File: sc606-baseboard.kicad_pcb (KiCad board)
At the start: 6 copper layers, 100 x 80 mm, 479 parts, among them IC1 TPS54561DPRT, IC2 TPS7A0518PDBVT, IC3 TPS7A0518PDBVT, J1 1053131102, J10 E8124-015-01, J11 E8124-015-01, J12 E8124-015-01, J14 CONMMCX002-SMD-T, J2 WE_68715014522, J3 F52R-1A7H1-11020, J4 46756-1001, J5 U_FL-R-SMT-1_10_, J6 E8124-015-01, J7 DM3AT-SF-PEJM5, J8 693022010811, J9 E8124-015-01, M1 SC606T, Q1 BSS138APW, Q10 Si7223DN, Q11 Si7223DN, Q2 BSS138-7-F, Q3 BSS138APW, Q4 BSS138APW, Q5 BSS138APW, Q6 BSS138APW, Q7 BSS138-7-F, Q8 BSS138-7-F, Q9 SQS401EN-T1_BE3, SW1 1X03, U1 AP62301WU-7, U10 NCP163ASN330T1G, U11 EMIF06-MSD02N16, U12 STUSB4500QTR, U13 FT232RQ-REEL, U14 LTC4418IUF#PBF, U15 USB57442G, U2 AP62301WU-7, U3 AP62301WU-7, U4 74LVC1G123GN, U5 NTS0102GT, U6 PCA9547BS, U7 LT9611UXC, U8 NTS0102GT, U9 FSUSB30UMX, Y1 ABM8G-24.000MHZ-18-D2Y-T, Y2 ABM8G-25.000MHZ-B4Y-T

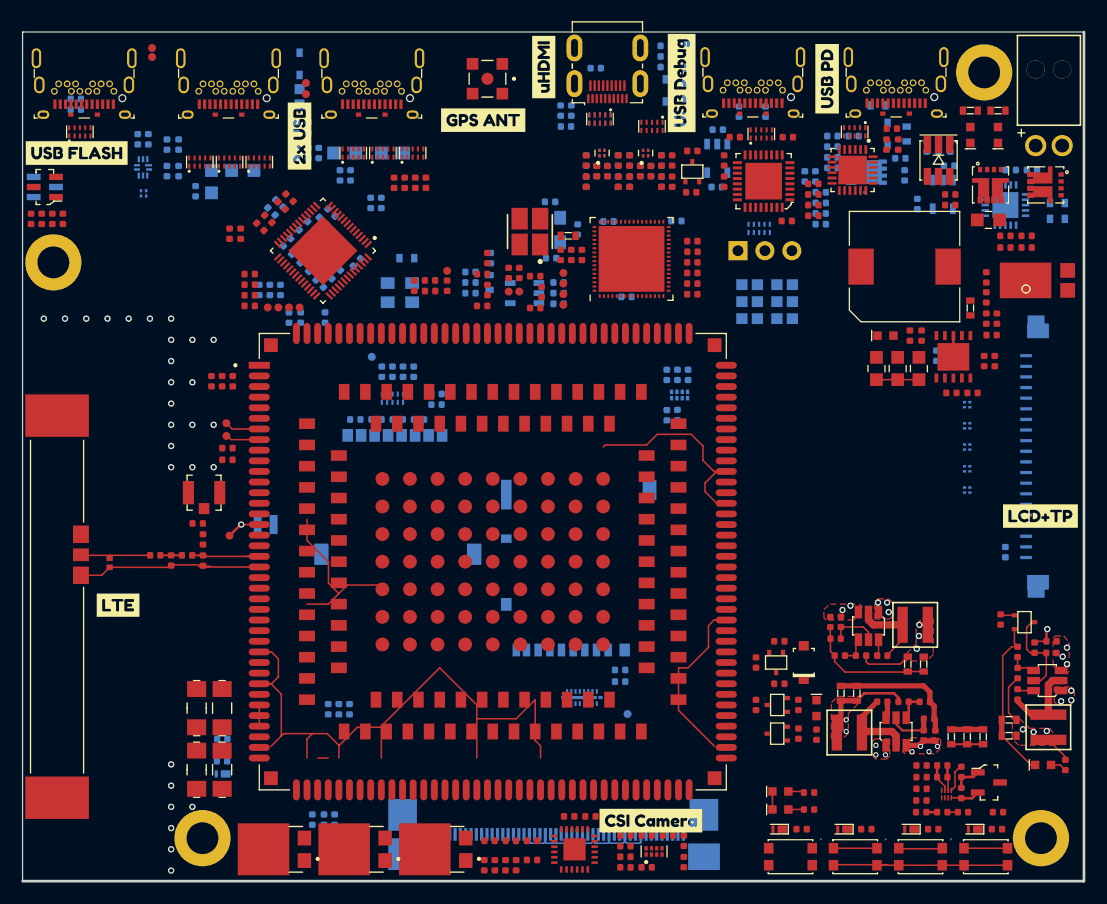
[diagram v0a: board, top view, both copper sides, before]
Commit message: Adjusted position of uHDMI
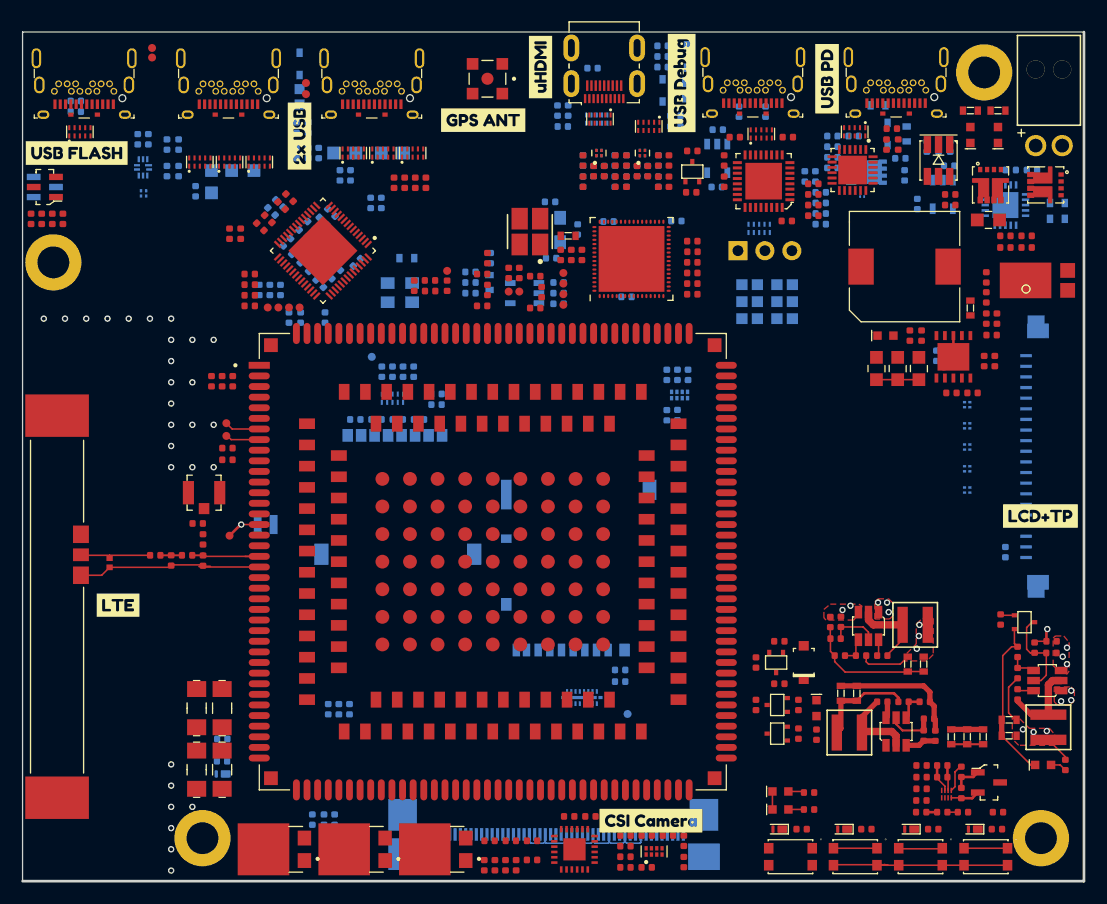
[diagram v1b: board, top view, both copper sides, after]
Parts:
- moved D35 0.40 mm to (154.7, 57.9)
- moved C75 0.30 mm to (133.5, 55.5)
- moved C76 0.30 mm to (134.5, 55.5)
- moved C77 0.30 mm to (133.5, 55.5)
- moved C78 0.30 mm to (134.5, 55.5)
- moved C81 0.30 mm to (135.5, 54.5)
- moved C82 0.30 mm to (135.5, 56.5)
- moved D30 0.30 mm to (129.7, 50.6)
- moved D6 0.30 mm to (134.6, 51.3)
- moved L18 0.30 mm to (134.0, 53.8)
- moved L19 0.30 mm to (134.0, 53.8)
- moved R61 0.30 mm to (137.1, 51.3)
- moved R62 0.30 mm to (137.1, 50.3)
- moved R64 0.30 mm to (131.4, 56.5)
- moved R67 0.30 mm to (132.5, 56.5)
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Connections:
- Q11 pad 5: (no net) -> VDD
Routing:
- net GND: track 219.1 -> 105.8 mm, vias 32 -> 29
- net (no net): track 2.00 -> 0.00 mm
- net USB_VBUS: track 1.00 -> 0.00 mm
- net 5V0_SYS: vias 9 -> 5
- net 3V3_SYS: vias 2 -> 0
- removed copper zone on F.Cu, net 3V3_SYS

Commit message: Modified position of buttons, SD, SIM and USB connectors. Modified LT9611 footprint
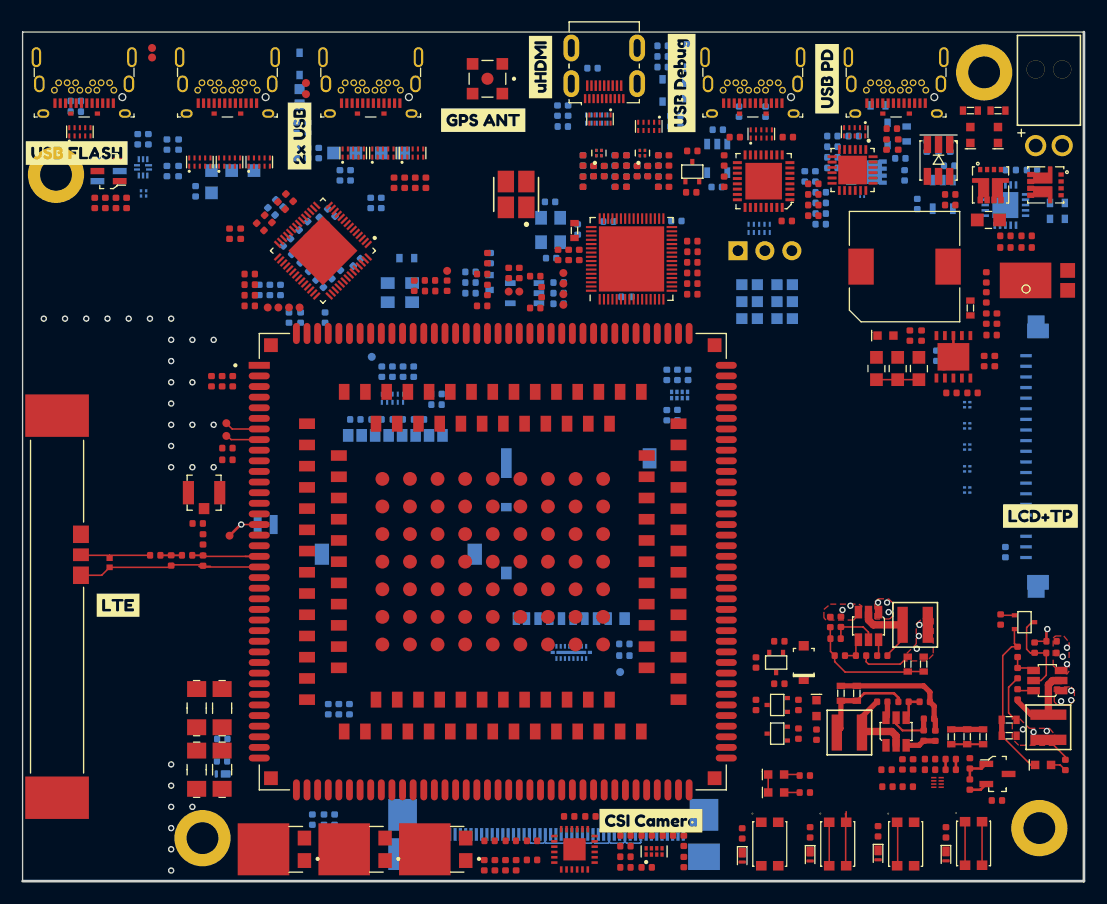
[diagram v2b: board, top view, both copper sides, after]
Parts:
- moved MP3 8.25 mm to (78.8, 55.9)
- moved Q7 6.18 mm to (83.7, 55.5)
- moved Q8 6.18 mm to (83.7, 55.5)
- moved R108 6.18 mm to (85.4, 58.5)
- moved R109 6.18 mm to (83.4, 58.5)
- moved R110 6.18 mm to (84.4, 58.5)
- moved R111 6.18 mm to (82.4, 58.5)
- moved R24 5.73 mm to (159.0, 113.5)
- moved R21 5.70 mm to (157.1, 113.5)
- moved R162 5.61 mm to (143.4, 117.9), turned to 270 degrees
- moved R96 5.31 mm to (149.8, 117.8), turned to 270 degrees
- moved R95 5.20 mm to (156.2, 117.7), turned to 270 degrees
- moved R22 5.16 mm to (157.0, 111.9), turned to 180 degrees
- moved R97 4.81 mm to (162.6, 117.8), turned to 270 degrees
- moved U11 4.37 mm to (127.3, 100.8)
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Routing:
- net GND: track 105.8 -> 97.4 mm
- net Net-(R25-Pad1): track 2.69 -> 0.00 mm
- net Net-(C37-Pad2): track 2.65 -> 1.22 mm
- net Net-(C37-Pad1): track 2.41 -> 1.29 mm
- net Net-(R21-Pad2): track 1.01 -> 0.00 mm
- net 5V0_SYS: track 7.70 -> 6.72 mm

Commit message: Changed ESD diode and transistor near USB-PD
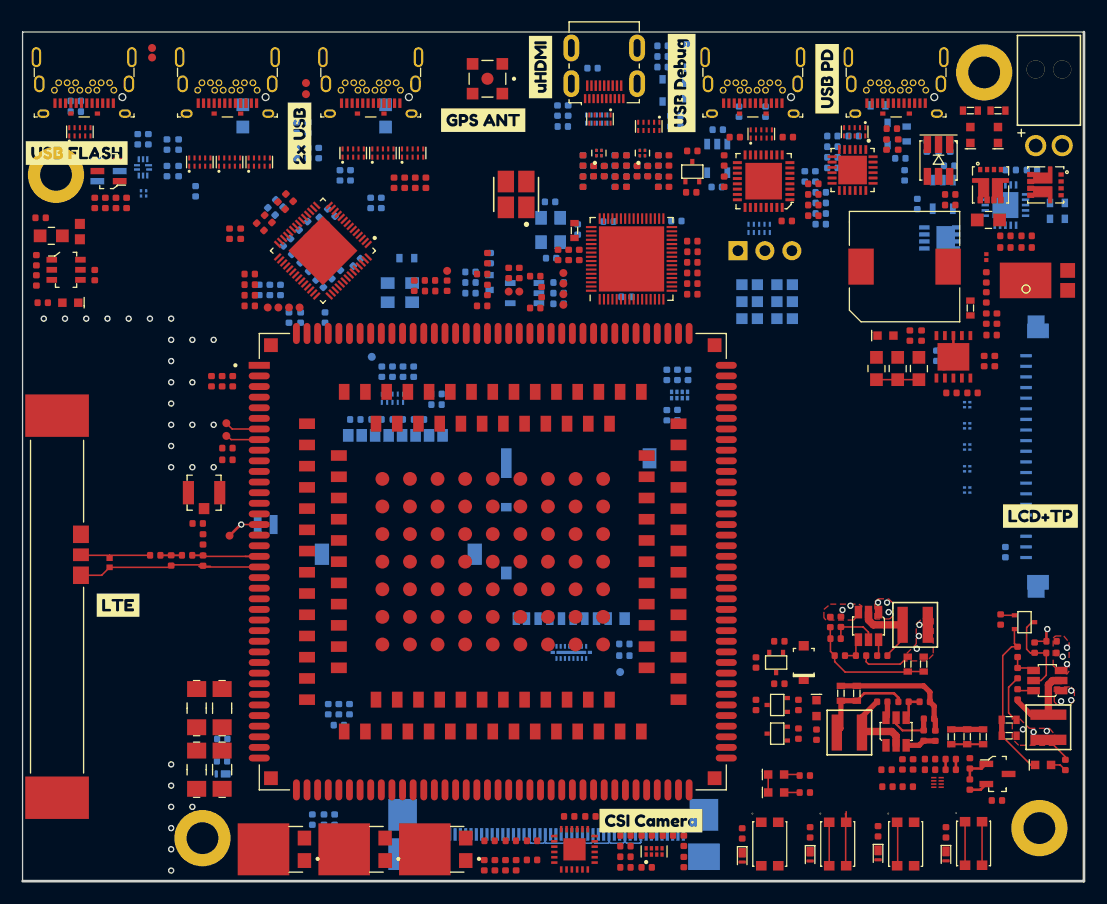
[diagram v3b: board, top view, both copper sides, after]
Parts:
- removed C138, C169: C_100u_0805, sc606-baseboard-footprints:0805-cap
- added C160: C_10u_0402, antmicro-footprints:0402-cap, F.Cu at (76.9, 63.9)
- added C161: C_100u_0805, antmicro-footprints:0805-cap, F.Cu at (78.3, 61.6)
- added IC4: AP22652W6-7, antmicro-footprints:SOT-23-6, F.Cu at (79.7, 64.8)
- added R170: R_0R_0402, antmicro-footprints:0402-res, B.Cu at (105.4, 107.7)
- added R171: R_10k_0402, antmicro-footprints:0402-res, F.Cu at (76.9, 65.8)
- added R172: R_470R_0402, antmicro-footprints:0402-res, F.Cu at (77.5, 67.9)
- added R173: R_12k4_0402, antmicro-footprints:0402-res, F.Cu at (82.4, 65.3)
- added R174: R_0R_0402, antmicro-footprints:0402-res, F.Cu at (77.3, 59.9)
- D24: value 1N4148WS -> KP-1608EC; footprint sc606-baseboard-footprints:SOD-323F -> sc606-baseboard-footprints:LED_0603; moved to F.Cu
- D35: value ESD144B1W0201E6327XTSA1 -> PESD18VF1BSFYL; footprint sc606-baseboard-footprints:ESD144B1W0201E6327XTSA1 -> antmicro-footprints:RESC0603X26N; moved to F.Cu
- FB2: footprint sc606-baseboard-footprints:0603 -> antmicro-footprints:0603; moved to F.Cu
- Q9: footprint sc606-baseboard-footprints:Vishay_PowerPAK_1212-8_Single -> antmicro-footprints:Vishay_PowerPAK_1212-8_Single
- moved D24 31.2 mm to (80.1, 67.9), turned to 180 degrees
- moved FB2 24.3 mm to (81.0, 61.2), turned to 90 degrees
- moved D35 13.0 mm to (166.4, 63.6), turned to 270 degrees
- moved Q9 9.28 mm to (162.0, 61.8)
- moved C170 5.15 mm to (96.3, 50.3), turned to 90 degrees
- moved C139 3.56 mm to (109.8, 50.3), turned to 90 degrees
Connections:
- FB2 pad 1: Net-(D24-PadK) -> Net-(C161-Pad1)
- M1 pad 168: (no net) -> Net-(M1-Pad168)
- Q9 pad 1: PD_VDD -> /USB-PD/PD_VBUS
- Q9 pad 2: PD_VDD -> /USB-PD/PD_VBUS
- Q9 pad 3: PD_VDD -> /USB-PD/PD_VBUS
- Q9 pad 5: /USB-PD/PD_VBUS -> PD_VDD

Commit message: Connected differential signals from camera modules and LCD display. Without checking track lengths
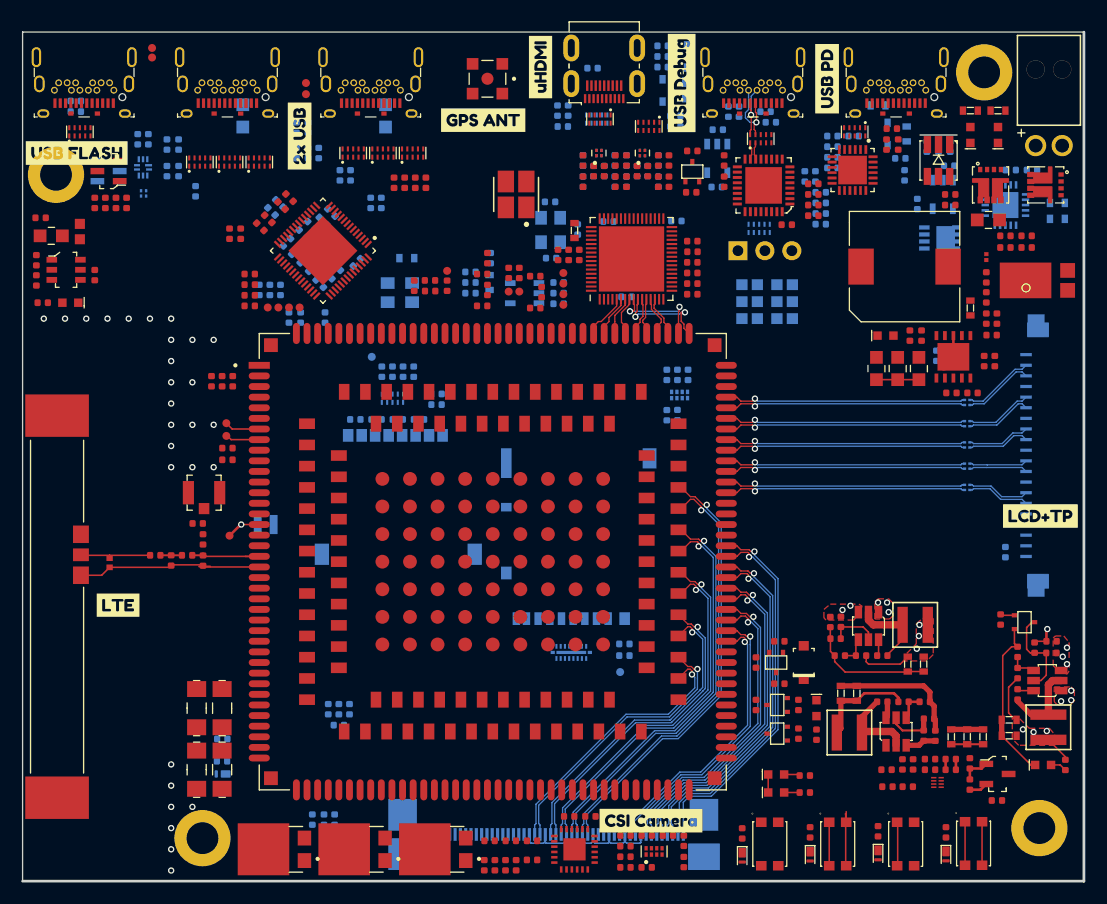
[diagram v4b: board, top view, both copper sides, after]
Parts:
- C112, C114: moved to B.Cu
- C156, C157, C159, C160: footprint antmicro-footprints:0402-cap -> sc606-baseboard-footprints:0402-cap
- C158, R161, R163, R165, R166, R170, R171, R172, R173, R174: footprint antmicro-footprints:0402-res -> sc606-baseboard-footprints:0402-res
- C161: footprint antmicro-footprints:0805-cap -> sc606-baseboard-footprints:0805-cap
- D35: footprint antmicro-footprints:RESC0603X26N -> sc606-baseboard-footprints:RESC0603X26N
- FB2: footprint antmicro-footprints:0603 -> sc606-baseboard-footprints:0603
- IC4: footprint antmicro-footprints:SOT-23-6 -> sc606-baseboard-footprints:SOT-23-6
- J1: footprint antmicro-footprints:1053131102 -> sc606-baseboard-footprints:1053131102
- Q9: footprint antmicro-footprints:Vishay_PowerPAK_1212-8_Single -> sc606-baseboard-footprints:Vishay_PowerPAK_1212-8_Single
- R164, R167, R168, R169: footprint antmicro-footprints:0603-res -> sc606-baseboard-footprints:0603-res
- U14: footprint antmicro-footprints:QFN-20_1EP_4x4_P0.5mm -> sc606-baseboard-footprints:QFN-20_1EP_4x4_P0.5mm
- moved C114 3.76 mm to (145.6, 49.9), turned to 0 degrees
- moved C143 3.50 mm to (142.1, 49.9)
- moved C112 2.13 mm to (146.1, 50.9)
- moved D21 0.45 mm to (145.2, 52.5)
- moved U13 0.40 mm to (144.9, 56.4)
- moved C113 0.35 mm to (147.6, 60.5)
- moved L11 0.25 mm to (164.6, 83.3)
- moved L12 0.25 mm to (164.6, 85.3)
- moved L8 0.21 mm to (164.6, 77.3)
- moved L10 0.20 mm to (164.6, 81.3)
- moved L9 0.20 mm to (164.6, 79.3)
- moved J3 0.10 mm to (172.6, 82.3)
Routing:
- net CAM2_D3_N: track 0.00 -> 41.1 mm, vias 0 -> 1
- net CAM2_D3_P: track 0.00 -> 40.7 mm, vias 0 -> 1
- net CAM2_D2_N: track 0.00 -> 37.6 mm, vias 0 -> 1
- net CAM2_D2_P: track 0.00 -> 37.2 mm, vias 0 -> 1
- net CAM1_D3_N: track 0.00 -> 35.4 mm, vias 0 -> 1
- net CAM1_D3_P: track 0.00 -> 35.1 mm, vias 0 -> 1
- net CAM2_D1_N: track 0.00 -> 33.8 mm, vias 0 -> 1
- net CAM1_D2_N: track 0.00 -> 33.4 mm, vias 0 -> 1
- net CAM2_D1_P: track 0.00 -> 33.4 mm, vias 0 -> 1
- net CAM1_D2_P: track 0.00 -> 33.0 mm, vias 0 -> 1
- net CAM1_D1_N: track 0.00 -> 31.3 mm, vias 0 -> 1
- net CAM1_D1_P: track 0.00 -> 30.9 mm, vias 0 -> 1
- net CAM2_D0_N: track 0.00 -> 30.0 mm, vias 0 -> 1
- net CAM2_D0_P: track 0.00 -> 29.6 mm, vias 0 -> 1
- net CAM1_D0_N: track 0.00 -> 29.2 mm, vias 0 -> 1
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
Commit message: Routed CAM, LCD, USB Debug differential pairs with tuning
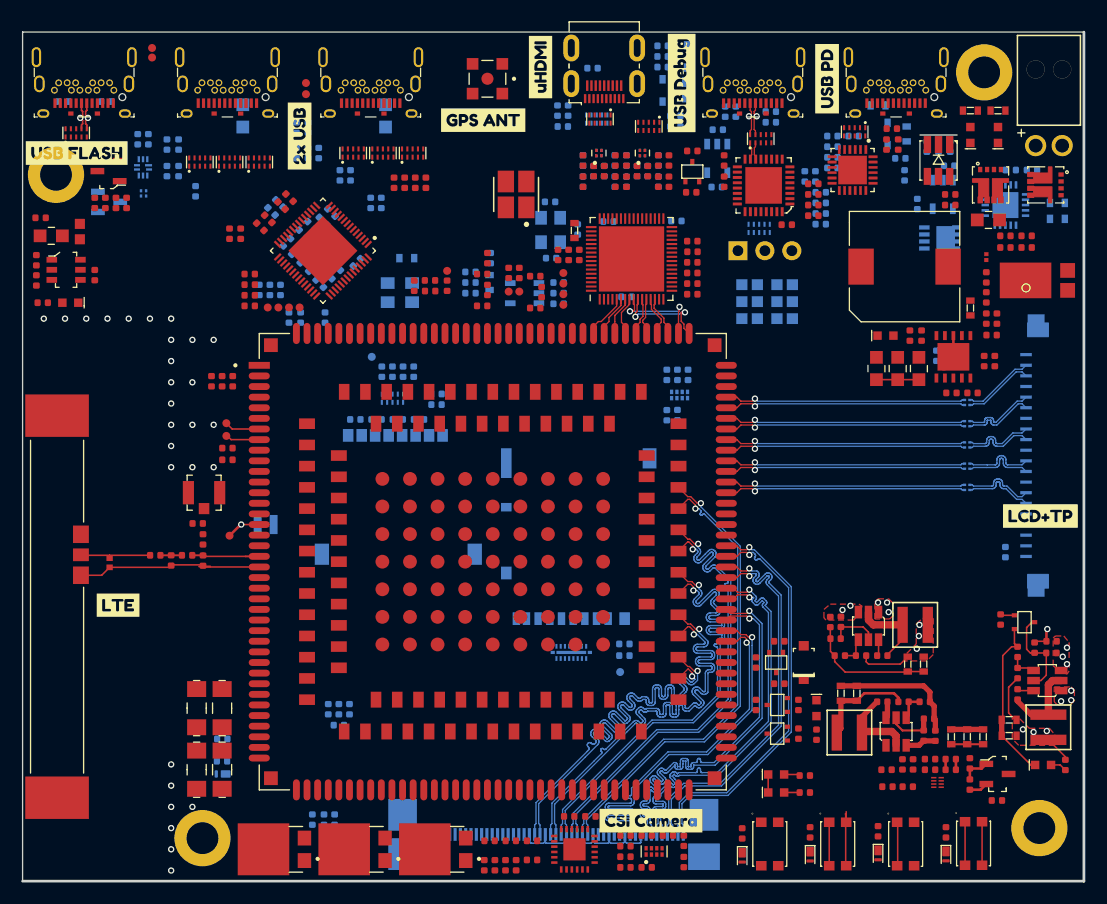
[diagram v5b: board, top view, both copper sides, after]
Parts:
- moved C110 3.04 mm to (83.5, 49.0), turned to 0 degrees
- moved Q8 2.90 mm to (83.8, 58.4)
- moved C109 1.17 mm to (79.5, 49.0)
- moved C114 0.50 mm to (146.1, 49.9)
- moved D20 0.36 mm to (80.7, 51.9)
- moved C142 0.30 mm to (142.8, 49.9)
- moved C143 0.30 mm to (141.8, 49.9)
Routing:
- net CAM2_CLK_P: track 25.8 -> 43.8 mm
- net CAM2_CLK_N: track 26.4 -> 43.8 mm
- net CAM2_D0_P: track 29.6 -> 43.8 mm
- net CAM2_D0_N: track 30.0 -> 43.8 mm
- net CAM1_CLK_P: track 26.3 -> 37.3 mm
- net CAM1_CLK_N: track 26.9 -> 37.3 mm
- net CAM2_D1_P: track 33.4 -> 43.8 mm
- net CAM2_D1_N: track 33.8 -> 43.8 mm
- net CAM1_D0_P: track 28.8 -> 37.7 mm
- net CAM1_D0_N: track 29.2 -> 37.7 mm
- net /USB_flash_debug/USB_FLASH_N: track 0.00 -> 8.31 mm, vias 0 -> 1
- net /USB_flash_debug/USB_FLASH_P: track 0.00 -> 8.31 mm, vias 0 -> 1
- net CAM1_D1_P: track 30.9 -> 37.7 mm
- net CAM2_D2_P: track 37.2 -> 43.7 mm
- net CAM1_D1_N: track 31.3 -> 37.7 mm
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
